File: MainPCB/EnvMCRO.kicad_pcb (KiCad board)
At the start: 2 copper layers, 109.6 x 69.7 mm, 30 parts, among them U1 Pico

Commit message: Added Mechboards logo for later use
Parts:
- removed G***: LOGO, Logo:logo
- added Ref**: Val**, Logo:logo, F.Cu at (157.8, 99.5)

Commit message: Added Pads/traces for 3535 SK6812 or WS2812B
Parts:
- added D1: SK6812, LED_SMD:LED_SK6812MINI_PLCC4_3.5x3.5mm_P1.75mm, F.Cu at (75.3, 57.7)
- added D10: SK6812, LED_SMD:LED_SK6812MINI_PLCC4_3.5x3.5mm_P1.75mm, F.Cu at (94.4, 105.2)
- added D11: SK6812, LED_SMD:LED_SK6812MINI_PLCC4_3.5x3.5mm_P1.75mm, F.Cu at (113.4, 105.2)
- added D12: SK6812, LED_SMD:LED_SK6812MINI_PLCC4_3.5x3.5mm_P1.75mm, F.Cu at (132.5, 105.2)
- added D2: SK6812, LED_SMD:LED_SK6812MINI_PLCC4_3.5x3.5mm_P1.75mm, F.Cu at (94.4, 57.7)
- added D3: SK6812, LED_SMD:LED_SK6812MINI_PLCC4_3.5x3.5mm_P1.75mm, F.Cu at (113.4, 57.8)
- added D4: SK6812, LED_SMD:LED_SK6812MINI_PLCC4_3.5x3.5mm_P1.75mm, F.Cu at (132.5, 57.8)
- added D5: SK6812, LED_SMD:LED_SK6812MINI_PLCC4_3.5x3.5mm_P1.75mm, F.Cu at (75.3, 81.5)
- added D6: SK6812, LED_SMD:LED_SK6812MINI_PLCC4_3.5x3.5mm_P1.75mm, F.Cu at (94.4, 81.5)
- added D7: SK6812, LED_SMD:LED_SK6812MINI_PLCC4_3.5x3.5mm_P1.75mm, F.Cu at (113.4, 81.5)
- added D8: SK6812, LED_SMD:LED_SK6812MINI_PLCC4_3.5x3.5mm_P1.75mm, F.Cu at (132.5, 81.5)
- added D9: SK6812, LED_SMD:LED_SK6812MINI_PLCC4_3.5x3.5mm_P1.75mm, F.Cu at (75.3, 105.2)
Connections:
- U1 pad 40: Net-(U1-Pad40) -> VBUS
- U1 pad 7: Net-(U1-Pad7) -> LEDDINPIN
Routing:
- net VBUS: track 0.00 -> 346.9 mm
- net Net-(D8-Pad4): track 0.00 -> 93.6 mm
- net Net-(D4-Pad4): track 0.00 -> 91.9 mm
- net LEDDINPIN: track 0.00 -> 84.3 mm
- net Net-(D1-Pad4): track 0.00 -> 16.9 mm
- net Net-(D2-Pad4): track 0.00 -> 16.9 mm
- net Net-(D3-Pad4): track 0.00 -> 16.8 mm
- net Net-(D7-Pad4): track 0.00 -> 16.7 mm
- net Net-(D6-Pad4): track 0.00 -> 16.7 mm
- net Net-(D5-Pad4): track 0.00 -> 16.7 mm
- net Net-(D10-Pad4): track 0.00 -> 16.6 mm
- net Net-(D11-Pad4): track 0.00 -> 16.6 mm
- net Net-(D10-Pad2): track 0.00 -> 16.6 mm
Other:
- board text removed: "http://github.com/Envious-Data/Env-MCRO"

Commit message: smol aesthetic tweak
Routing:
- net VBUS: track 346.9 -> 343.4 mm

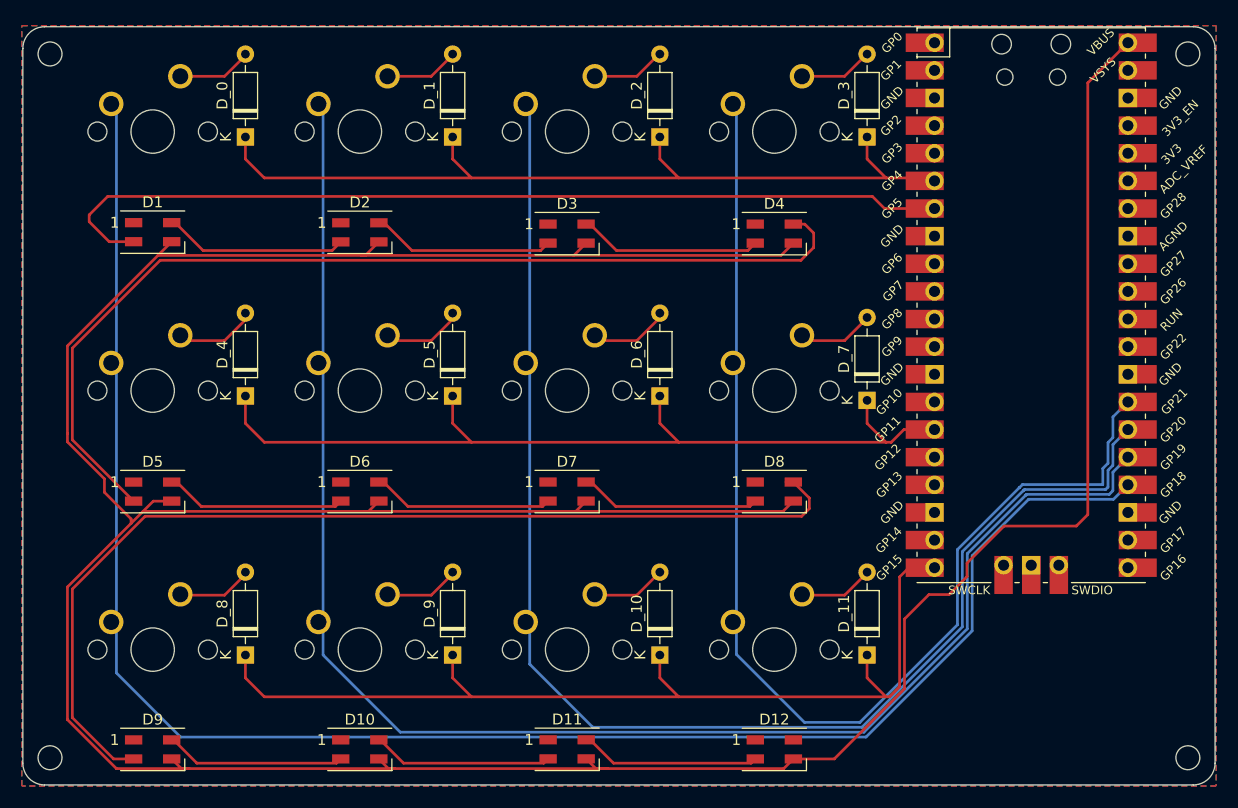
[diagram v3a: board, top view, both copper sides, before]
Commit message: better RGB implementation using SK6812 MINI E footprints to be installed reverse on the back of the PCB + generated gerber
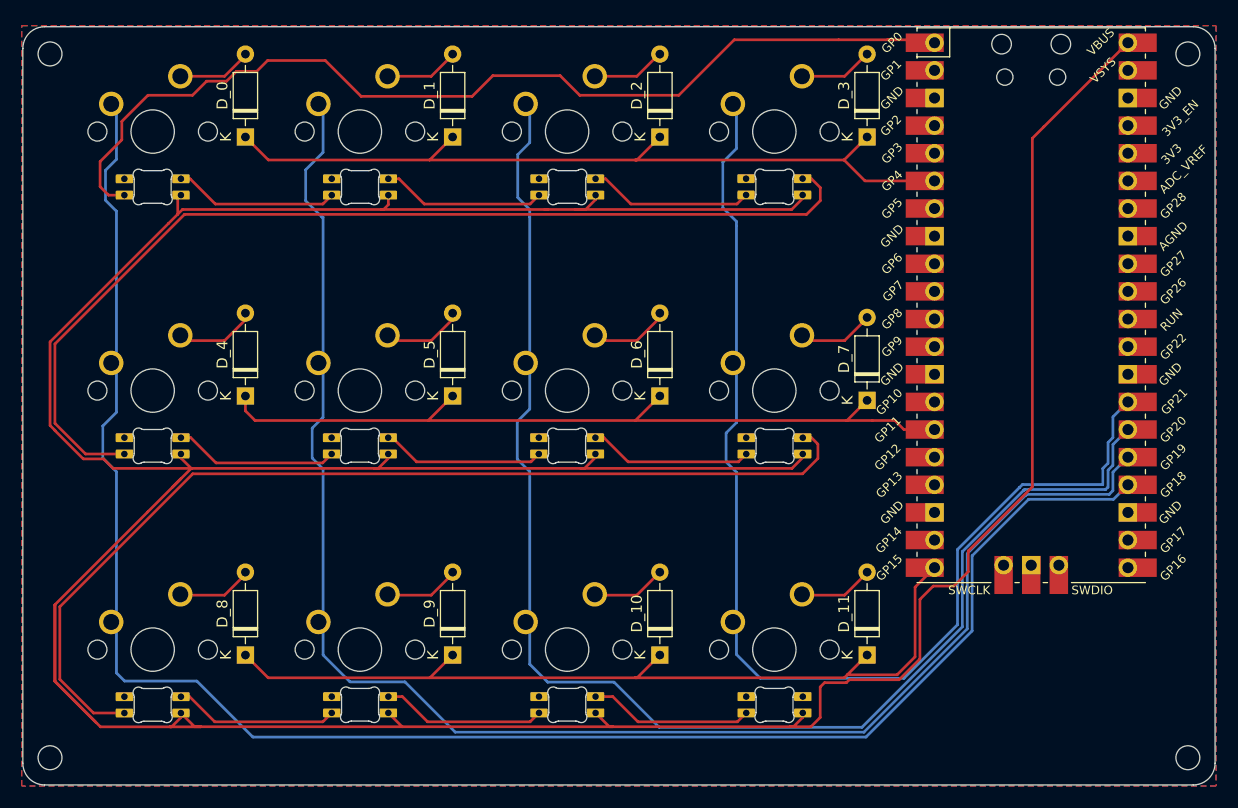
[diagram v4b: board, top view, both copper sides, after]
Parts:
- D1, D10, D11, D12, D2, D3, D4, D5, D6, D7, D8, D9: value SK6812 -> SK6812MINI-E; footprint LED_SMD:LED_SK6812MINI_PLCC4_3.5x3.5mm_P1.75mm -> sk6812mini:MX_SK6812MINI-E_REV
- moved D4 9.39 mm to (132.5, 48.4)
- moved D3 9.37 mm to (113.5, 48.5)
- moved D5 9.29 mm to (75.3, 72.2)
- moved D6 9.28 mm to (94.4, 72.2)
- moved D7 9.28 mm to (113.4, 72.2)
- moved D8 9.28 mm to (132.5, 72.2)
- moved D2 9.25 mm to (94.4, 48.5)
- moved D1 9.23 mm to (75.3, 48.5)
- moved D12 9.19 mm to (132.5, 96.0)
- moved D10 9.19 mm to (94.4, 96.0)
- moved D11 9.18 mm to (113.5, 96.0)
- moved D9 9.17 mm to (75.3, 96.1)
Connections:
- D1 pad 1: GND -> VBUS
- D1 pad 2: LEDDINPIN -> Net-(D1-Pad2)
- D1 pad 3: VBUS -> GND
- D1 pad 4: Net-(D1-Pad4) -> LEDDINPIN
- D10 pad 1: GND -> VBUS
- D10 pad 3: VBUS -> GND
- D11 pad 1: GND -> VBUS
- D11 pad 2: Net-(D10-Pad4) -> Net-(D11-Pad2)
- D11 pad 3: VBUS -> GND
- D11 pad 4: Net-(D11-Pad4) -> Net-(D10-Pad2)
- D12 pad 1: GND -> VBUS
- D12 pad 2: Net-(D11-Pad4) -> Net-(D12-Pad2)
- D12 pad 3: VBUS -> GND
- D12 pad 4: Net-(D12-Pad4) -> Net-(D11-Pad2)
- D2 pad 1: GND -> VBUS
- D2 pad 2: Net-(D1-Pad4) -> Net-(D2-Pad2)
- D2 pad 3: VBUS -> GND
- D2 pad 4: Net-(D2-Pad4) -> Net-(D1-Pad2)
- D3 pad 1: GND -> VBUS
- D3 pad 2: Net-(D2-Pad4) -> Net-(D3-Pad2)
- D3 pad 3: VBUS -> GND
- D3 pad 4: Net-(D3-Pad4) -> Net-(D2-Pad2)
- D4 pad 1: GND -> VBUS
- D4 pad 2: Net-(D3-Pad4) -> Net-(D4-Pad2)
- D4 pad 3: VBUS -> GND
- D4 pad 4: Net-(D4-Pad4) -> Net-(D3-Pad2)
- D5 pad 1: GND -> VBUS
- D5 pad 2: Net-(D4-Pad4) -> Net-(D5-Pad2)
- D5 pad 3: VBUS -> GND
- D5 pad 4: Net-(D5-Pad4) -> Net-(D4-Pad2)
- D6 pad 1: GND -> VBUS
- D6 pad 2: Net-(D5-Pad4) -> Net-(D6-Pad2)
- D6 pad 3: VBUS -> GND
- D6 pad 4: Net-(D6-Pad4) -> Net-(D5-Pad2)
- D7 pad 1: GND -> VBUS
- D7 pad 2: Net-(D6-Pad4) -> Net-(D7-Pad2)
- D7 pad 3: VBUS -> GND
- D7 pad 4: Net-(D7-Pad4) -> Net-(D6-Pad2)
- D8 pad 1: GND -> VBUS
- D8 pad 2: Net-(D7-Pad4) -> Net-(D8-Pad2)
- D8 pad 3: VBUS -> GND
- D8 pad 4: Net-(D8-Pad4) -> Net-(D7-Pad2)
- D9 pad 1: GND -> VBUS
- D9 pad 2: Net-(D8-Pad4) -> Net-(D10-Pad4)
- D9 pad 3: VBUS -> GND
- D9 pad 4: Net-(D10-Pad2) -> Net-(D8-Pad2)
- U1 pad 1: Net-(U1-Pad1) -> LEDDINPIN
- U1 pad 7: LEDDINPIN -> Net-(U1-Pad7)
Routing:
- net Net-(D4-Pad2): track 0.00 -> 93.8 mm
- net Net-(D8-Pad4): track 93.6 -> 0.00 mm
- net Net-(D8-Pad2): track 0.00 -> 92.2 mm
- net Net-(D4-Pad4): track 91.9 -> 0.00 mm
- net VBUS: track 343.4 -> 365.8 mm
- net Net-(D1-Pad4): track 16.9 -> 0.00 mm
- net Net-(D2-Pad4): track 16.9 -> 0.00 mm
- net Net-(D3-Pad4): track 16.8 -> 0.00 mm
- net Net-(D7-Pad4): track 16.7 -> 0.00 mm
- net Net-(D6-Pad4): track 16.7 -> 0.00 mm
- net Net-(D5-Pad4): track 16.7 -> 0.00 mm
- net Net-(D11-Pad4): track 16.6 -> 0.00 mm
- net Net-(D1-Pad2): track 0.00 -> 15.2 mm
- net Net-(D5-Pad2): track 0.00 -> 15.2 mm
- net Net-(D11-Pad2): track 0.00 -> 15.2 mm
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
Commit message: testing new graphic for the board.
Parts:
- removed Ref**: Val**, Logo:logo
- added REF**: RotaryEncoder_Alps_EC11E-Switch_Vertical_H20mm, Rotary_Encoder:RotaryEncoder_Alps_EC11E-Switch_Vertical_H20mm, F.Cu at (164.7, 102.6)
